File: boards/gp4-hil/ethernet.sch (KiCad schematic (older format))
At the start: 46 parts, among them J1 BEL_FUSE_0826-1G1T-23-F, U2 XC7A100T-1FTG256C, U5 KSZ9031RN, U7 25 MHz

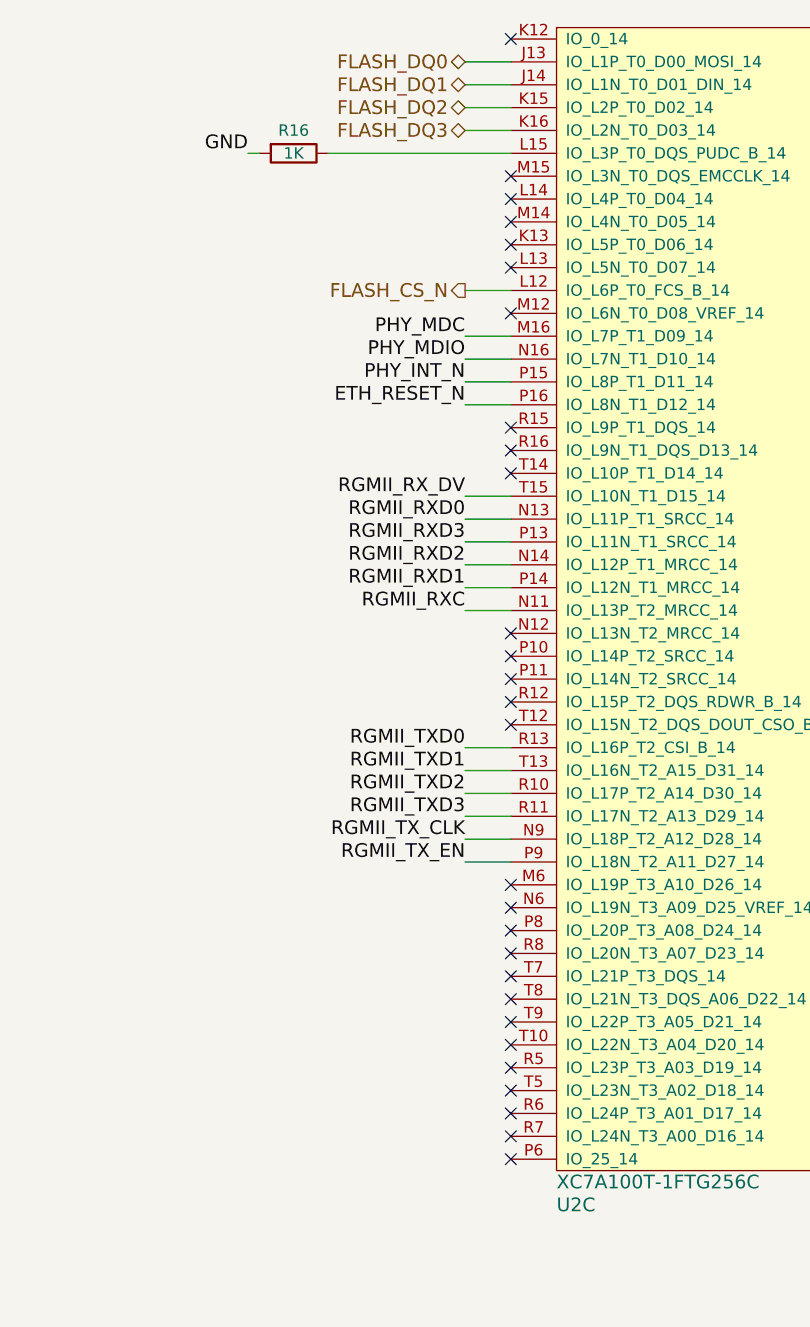
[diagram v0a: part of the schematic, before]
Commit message: Merged JTAG master stuff with Ethernet schematic page
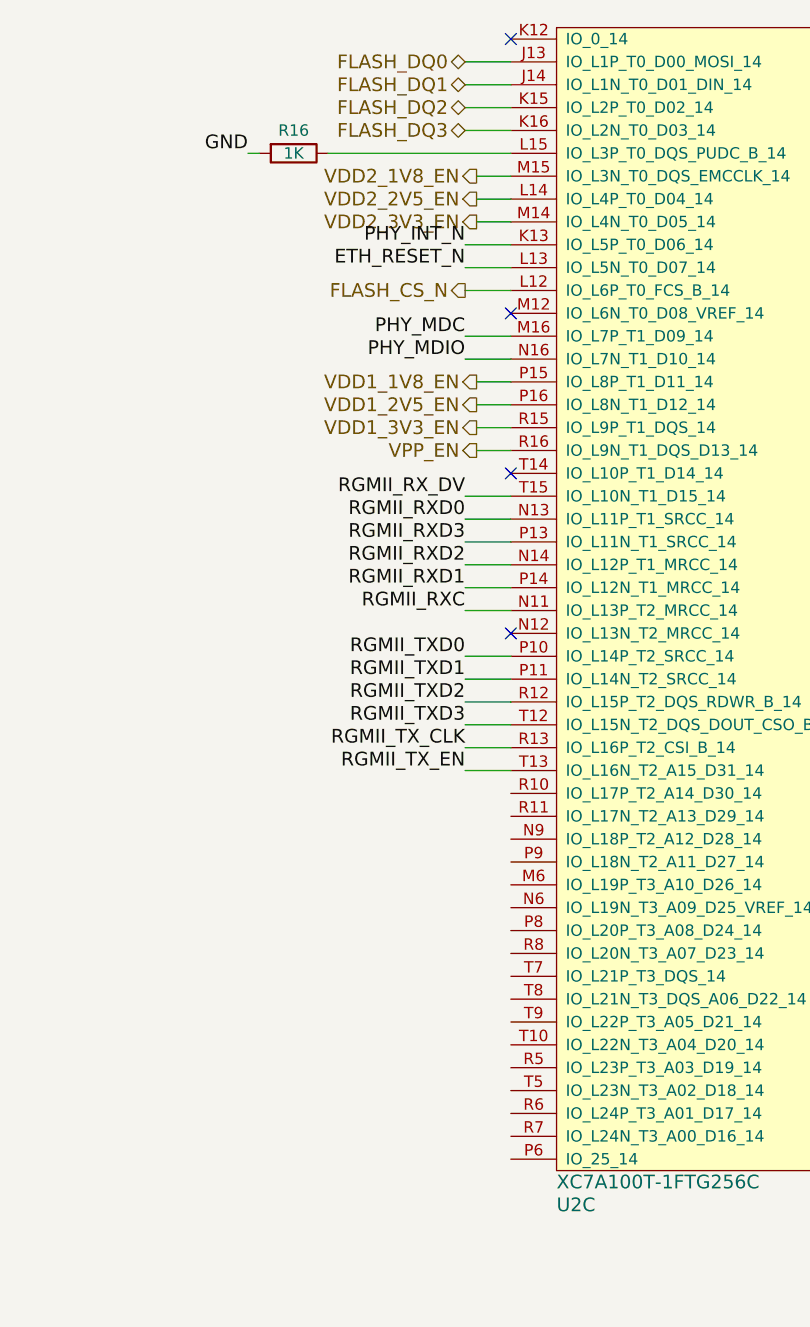
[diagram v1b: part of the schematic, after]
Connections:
- net ETH_RESET_N: now also U2.L13 (IO_L5N_T0_D07_14); no longer U2.P16 (IO_L8N_T1_D12_14)
- net PHY_INT_N: now also U2.K13 (IO_L5P_T0_D06_14); no longer U2.P15 (IO_L8P_T1_D11_14)
- net RGMII_TXD0: now also U2.P10 (IO_L14P_T2_SRCC_14); no longer U2.R13 (IO_L16P_T2_CSI_B_14)
- net RGMII_TXD1: now also U2.P11 (IO_L14N_T2_SRCC_14); no longer U2.T13 (IO_L16N_T2_A15_D31_14)
- net RGMII_TXD2: now also U2.R12 (IO_L15P_T2_DQS_RDWR_B_14); no longer U2.R10 (IO_L17P_T2_A14_D30_14)
- net RGMII_TXD3: now also U2.T12 (IO_L15N_T2_DQS_DOUT_CSO_B_14); no longer U2.R11 (IO_L17N_T2_A13_D29_14)
- net RGMII_TX_CLK: now also U2.R13 (IO_L16P_T2_CSI_B_14); no longer U2.N9 (IO_L18P_T2_A12_D28_14)
- net RGMII_TX_EN: now also U2.T13 (IO_L16N_T2_A15_D31_14); no longer U2.P9 (IO_L18N_T2_A11_D27_14)
- net VDD2_2V5_EN: now reaches U2.L14 (IO_L4P_T0_D04_14)
- net VDD2_3V3_EN: now reaches U2.M14 (IO_L4N_T0_D05_14)
- net VDD2_1V8_EN: now reaches U2.M15 (IO_L3N_T0_DQS_EMCCLK_14)
- net VDD1_3V3_EN: now reaches U2.R15 (IO_L9P_T1_DQS_14)
- net VPP_EN: now reaches U2.R16 (IO_L9N_T1_DQS_D13_14)
- new net VDD1_1V8_EN: U2.P15 (IO_L8P_T1_D11_14)
- new net VDD1_2V5_EN: U2.P16 (IO_L8N_T1_D12_14)
- no-connect marks 31 -> 7
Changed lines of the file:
@@
 $Descr A2 23386 16535
 encoding utf-8
-Sheet 3 8
+Sheet 3 7
 Title "GreenPak Hardware-In-Loop Test Platform"
 Date "2016-05-15"
 Rev "0.1"
 Comp "Andrew Zonenberg"
-Comment1 "Ethernet PHY"
+Comment1 "Ethernet PHY and JTAG masters"
 Comment2 ""
 Comment3 ""
@@
 GND
 Connection ~ 1150 5350
-$Comp
-L XC7AxT-xFTG256x U?
-U 3 1 57349080
-P 16400 9900
-AR Path="/57316B0C/57349080" Ref="U?"  Part="1"
-AR Path="/57316A40/57349080" Ref="U2"  Part="3"
-F 0 "U2" H 16400 9700 60  0000 L CNN
-F 1 "XC7A100T-1FTG256C" H 16400 9800 60  0000 L CNN
-F 2 "" H 16400 9900 60  0000 C CNN
-F 3 "" H 16400 9900 60  0000 C CNN
-	3    16400 9900
-	1    0    0    -1
-$EndComp
 Wire Wire Line
 	8850 8400 8850 8500
@@
 Text Label 16000 6400 2    60   ~ 0
 PHY_MDIO
-Text Label 16000 6500 2    60   ~ 0
+Text Label 16000 5900 2    60   ~ 0
 PHY_INT_N
+Text Label 16000 7700 2    60   ~ 0
+RGMII_TXD0
+Text Label 16000 7800 2    60   ~ 0
+RGMII_TXD1
+Text Label 16000 7900 2    60   ~ 0
+RGMII_TXD2
+Text Label 16000 8000 2    60   ~ 0
+RGMII_TXD3
 Text Label 16000 8100 2    60   ~ 0
-RGMII_TXD0
+RGMII_TX_CLK
 Text Label 16000 8200 2    60   ~ 0
-RGMII_TXD1
-Text Label 16000 8300 2    60   ~ 0
-RGMII_TXD2
-Text Label 16000 8400 2    60   ~ 0
-RGMII_TXD3
-Text Label 16000 8500 2    60   ~ 0
-RGMII_TX_CLK
-Text Label 16000 8600 2    60   ~ 0
 RGMII_TX_EN
-Text Label 16000 6600 2    60   ~ 0
+Text Label 16000 6000 2    60   ~ 0
 ETH_RESET_N
 Wire Wire Line
@@
 Wire Wire Line
 	16000 7000 16200 7000
-NoConn ~ 16200 7600
 Wire Wire Line
 	16000 7400 16200 7400
@@
 	16000 6400 16200 6400
 Wire Wire Line
-	16000 6500 16200 6500
-Wire Wire Line
-	16000 6600 16200 6600
-Wire Wire Line
-	16000 8100 16200 8100
-Wire Wire Line
-	16000 8600 16200 8600
-Wire Wire Line
-	16200 8500 16000 8500
-Wire Wire Line
-	16000 8400 16200 8400
-Wire Wire Line
-	16200 8300 16000 8300
+	16000 5900 16200 5900
+Wire Wire Line
+	16000 6000 16200 6000
+Wire Wire Line
+	16000 7700 16200 7700
 Wire Wire Line
 	16000 8200 16200 8200
-NoConn ~ 16200 5900
-NoConn ~ 16200 5800
-NoConn ~ 16200 5700
-NoConn ~ 16200 5600
-NoConn ~ 16200 6700
-NoConn ~ 16200 6800
+Wire Wire Line
+	16200 8100 16000 8100
+Wire Wire Line
+	16000 8000 16200 8000
+Wire Wire Line
+	16200 7900 16000 7900
+Wire Wire Line
+	16000 7800 16200 7800
 NoConn ~ 16200 6900
-NoConn ~ 16200 9400
-NoConn ~ 16200 9300
-NoConn ~ 16200 9200
-NoConn ~ 16200 9100
-NoConn ~ 16200 9000
-NoConn ~ 16200 8900
-NoConn ~ 16200 8800
-NoConn ~ 16200 8700
 Text Notes 12050 3650 0    60   ~ 0
 TODO: FPGA core clock
@@
 Wire Wire Line
 	16000 6100 16200 6100
-NoConn ~ 16200 6000
 NoConn ~ 16200 6200
-NoConn ~ 16200 8000
-NoConn ~ 16200 7900
-NoConn ~ 16200 7800
-NoConn ~ 16200 7700
-NoConn ~ 16200 9500
-NoConn ~ 16200 9600
-NoConn ~ 16200 9700
-NoConn ~ 16200 9800
-NoConn ~ 16200 9900
+Text HLabel 16050 6700 0    60   Output ~ 0
+VDD1_3V3_EN
+Text HLabel 16050 6600 0    60   Output ~ 0
+VDD1_2V5_EN
+Text HLabel 16050 6500 0    60   Output ~ 0
+VDD1_1V8_EN
+Text HLabel 16050 5800 0    60   Output ~ 0
+VDD2_3V3_EN
+Text HLabel 16050 5700 0    60   Output ~ 0
+VDD2_2V5_EN
+Text HLabel 16050 5600 0    60   Output ~ 0
+VDD2_1V8_EN
+Text HLabel 16050 6800 0    60   Output ~ 0
+VPP_EN
+Wire Wire Line
+	16200 5600 16050 5600
+Wire Wire Line
+	16050 5700 16200 5700
+Wire Wire Line
+	16200 5800 16050 5800
+Wire Wire Line
+	16050 6500 16200 6500
+Wire Wire Line
+	16200 6600 16050 6600
+Wire Wire Line
+	16050 6700 16200 6700
+Wire Wire Line
+	16200 6800 16050 6800
+NoConn ~ 16200 7600
+$Comp
+L XC7AxT-xFTG256x U?
+U 3 1 57349080
+P 16400 9900
+AR Path="/57316B0C/57349080" Ref="U?"  Part="1"
+AR Path="/57316A40/57349080" Ref="U2"  Part="3"
+F 0 "U2" H 16400 9700 60  0000 L CNN
+F 1 "XC7A100T-1FTG256C" H 16400 9800 60  0000 L CNN
+F 2 "" H 16400 9900 60  0000 C CNN
+F 3 "" H 16400 9900 60  0000 C CNN
+	3    16400 9900
+	1    0    0    -1
+$EndComp
 $EndSCHEMATC

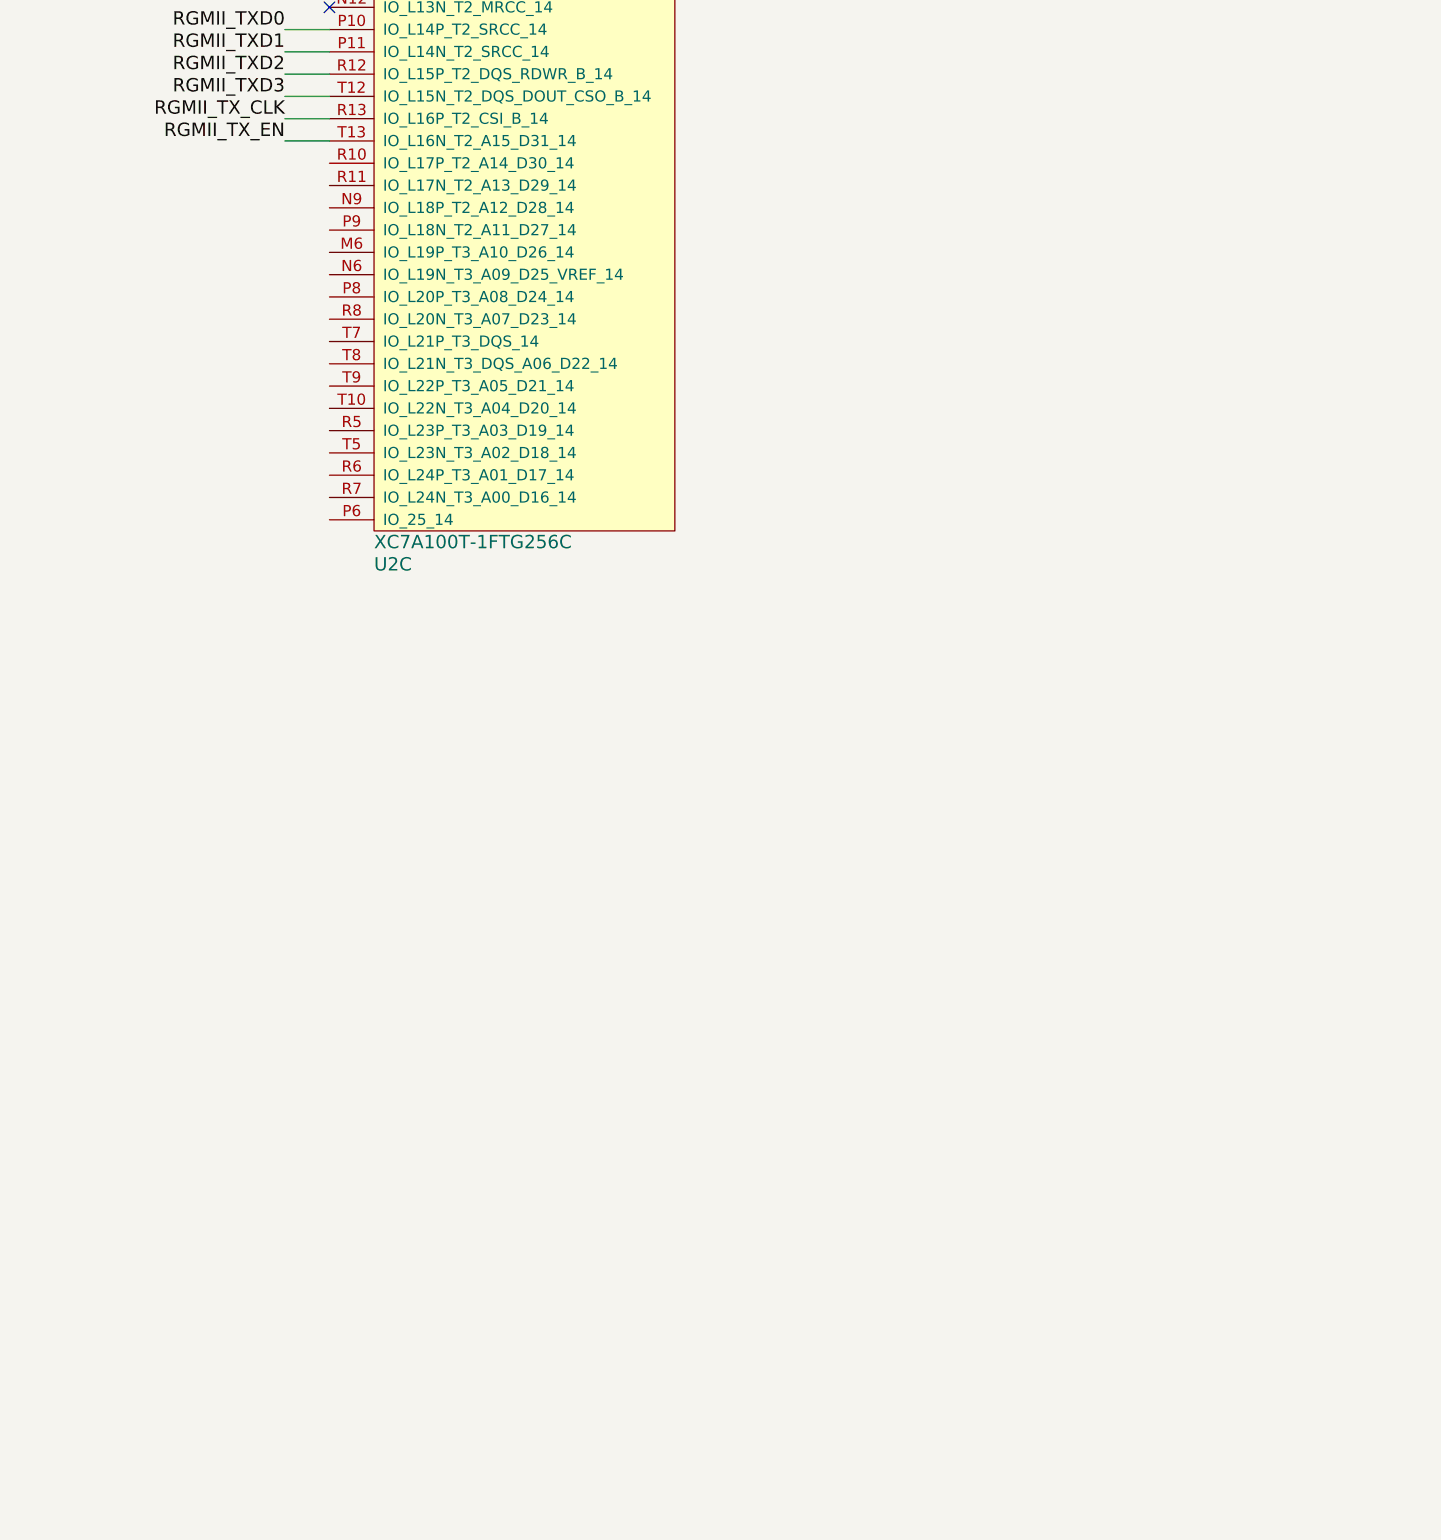
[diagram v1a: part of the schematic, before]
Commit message: Continued schematic capture, added JTAG master interfaces
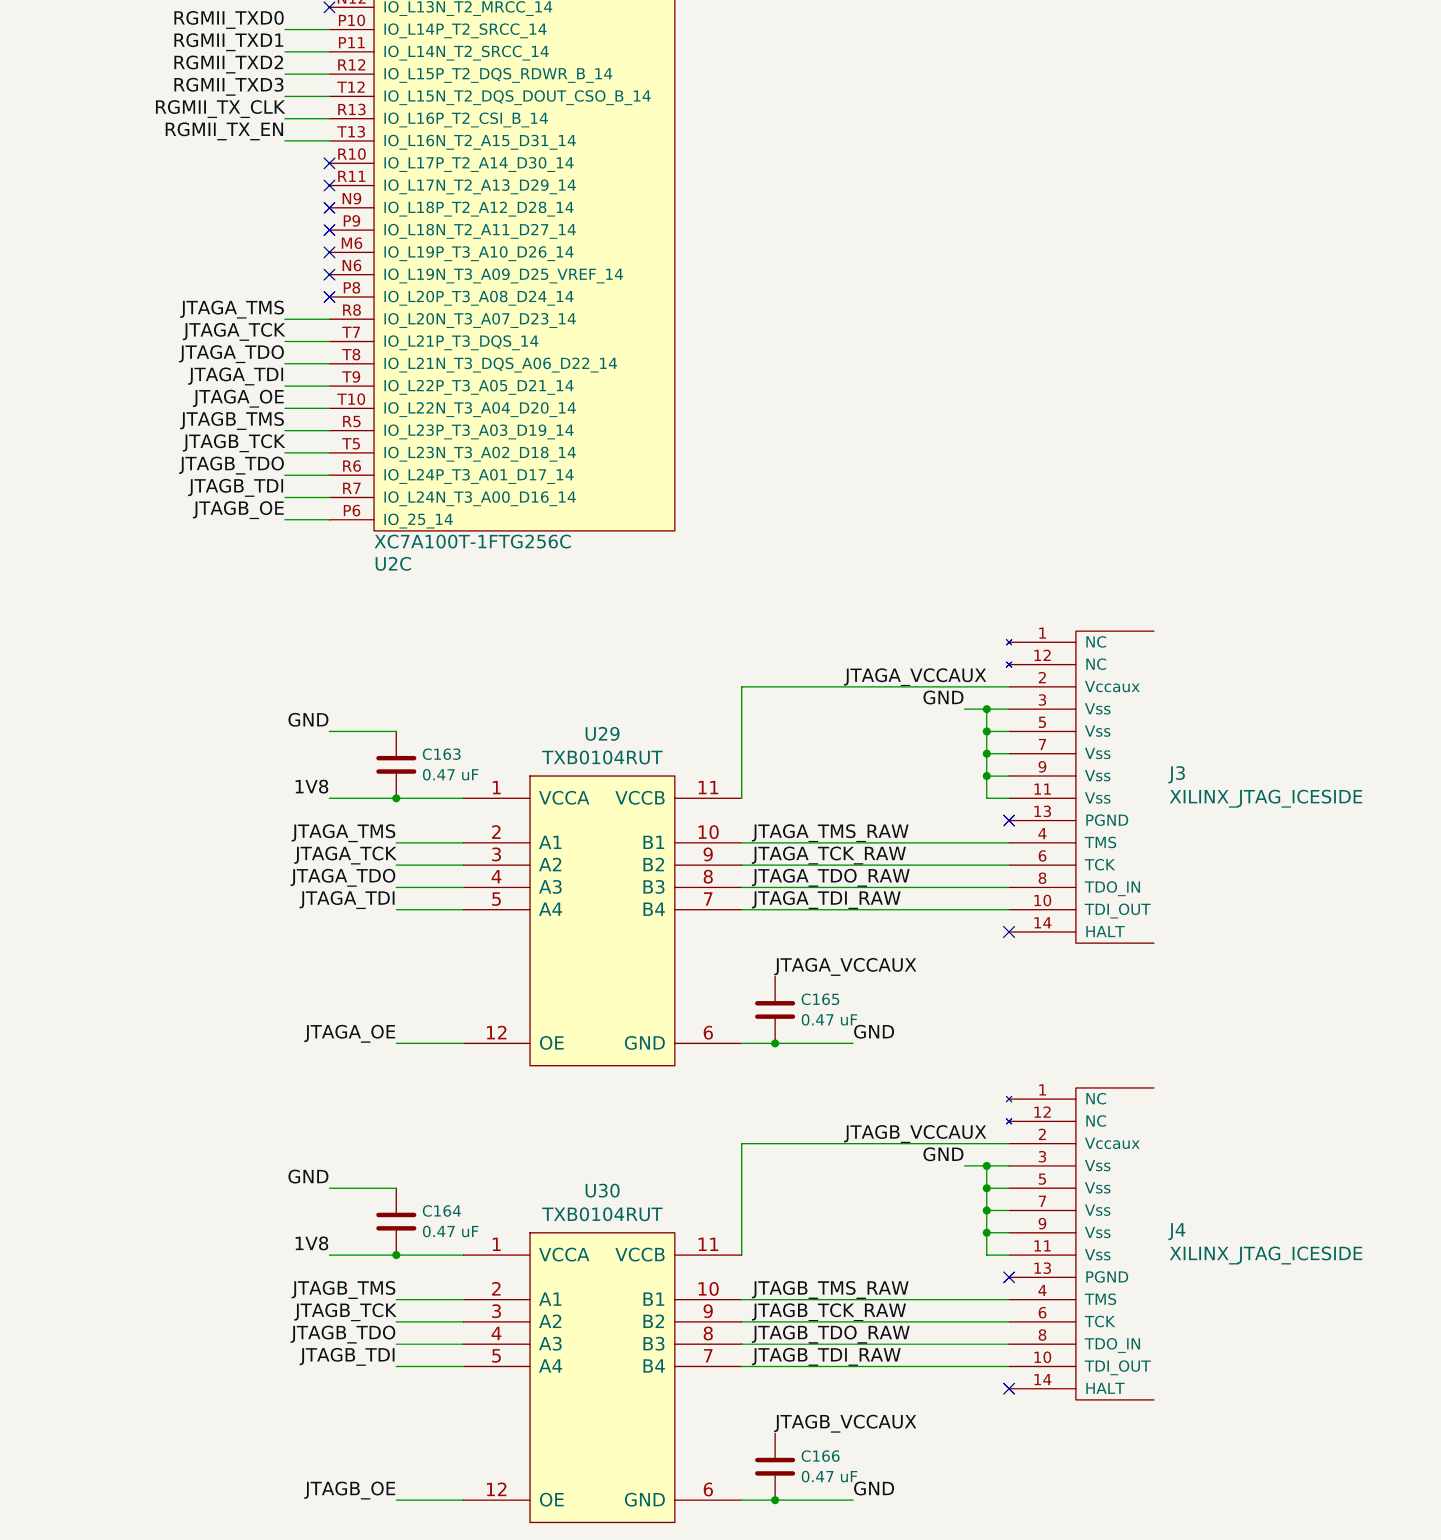
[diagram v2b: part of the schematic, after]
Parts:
- added C163, C164, C165, C166: 0.47 uF, symbol C
- added J3, J4: XILINX_JTAG_ICESIDE, symbol XILINX_JTAG_ICESIDE
- added U29, U30: TXB0104RUT, symbol TXB0104RUT
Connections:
- net 1V8: now also C163.2, C164.2, U29.1 (VCCA), U30.1 (VCCA)
- net GND: now also C163.1, C164.1, C165.2, C166.2, J3.11 (Vss), J3.3 (Vss), J3.5 (Vss), J3.7 (Vss), J3.9 (Vss), J4.11 (Vss), J4.3 (Vss), J4.5 (Vss), J4.7 (Vss), J4.9 (Vss), U29.6 (GND), U30.6 (GND)
- net JTAGB_OE: now reaches U2.P6 (IO_25_14)
- net JTAGB_OE: now also U30.12 (OE)
- net JTAGB_TMS: now reaches U2.R5 (IO_L23P_T3_A03_D19_14)
- net JTAGB_TMS: now also U30.2 (A1)
- net JTAGB_TDO: now reaches U2.R6 (IO_L24P_T3_A01_D17_14)
- net JTAGB_TDO: now also U30.4 (A3)
- net JTAGB_TDI: now reaches U2.R7 (IO_L24N_T3_A00_D16_14)
- net JTAGB_TDI: now also U30.5 (A4)
- net JTAGA_TMS: now reaches U2.R8 (IO_L20N_T3_A07_D23_14)
- net JTAGA_TMS: now also U29.2 (A1)
- net JTAGA_OE: now reaches U2.T10 (IO_L22N_T3_A04_D20_14)
- net JTAGA_OE: now also U29.12 (OE)
- net JTAGB_TCK: now reaches U2.T5 (IO_L23N_T3_A02_D18_14)
- net JTAGB_TCK: now also U30.3 (A2)
- net JTAGA_TCK: now reaches U2.T7 (IO_L21P_T3_DQS_14)
- net JTAGA_TCK: now also U29.3 (A2)
- net JTAGA_TDO: now reaches U2.T8 (IO_L21N_T3_DQS_A06_D22_14)
- net JTAGA_TDO: now also U29.4 (A3)
- net JTAGA_TDI: now reaches U2.T9 (IO_L22P_T3_A05_D21_14)
- net JTAGA_TDI: now also U29.5 (A4)
- new net JTAGA_TCK_RAW: J3.6 (TCK), U29.9 (B2)
- new net JTAGA_TDI_RAW: J3.10 (TDI_OUT), U29.7 (B4)
- new net JTAGA_TDO_RAW: J3.8 (TDO_IN), U29.8 (B3)
- new net JTAGA_TMS_RAW: J3.4 (TMS), U29.10 (B1)
- new net JTAGA_VCCAUX: C165.1, J3.2 (Vccaux), U29.11 (VCCB)
- new net JTAGB_TCK_RAW: J4.6 (TCK), U30.9 (B2)
- new net JTAGB_TDI_RAW: J4.10 (TDI_OUT), U30.7 (B4)
- new net JTAGB_TDO_RAW: J4.8 (TDO_IN), U30.8 (B3)
- new net JTAGB_TMS_RAW: J4.4 (TMS), U30.10 (B1)
- new net JTAGB_VCCAUX: C166.1, J4.2 (Vccaux), U30.11 (VCCB)
- no-connect marks 7 -> 18

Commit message: Added FPGA core clock, GPIO indicator LEDs, expansion header, lots of test points
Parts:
- added C175: 0.47 uF, symbol C
- added R150: 33, symbol R
- added TP22, TP23: TESTPOINT, symbol CONN_01X01
- added U33: 125 MHz, symbol OSC
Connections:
- net 1V8: now also C175.1, U33.1 (E/D#), U33.4 (Vdd)
- net GND: now also C175.2, U33.2 (Vss)
- net PHY_CLK_25MHZ: now also TP22.1 (P1)
- net RGMII_RXD0: now also U2.R16 (IO_L9N_T1_DQS_D13_14); no longer U2.N13 (IO_L11P_T1_SRCC_14)
- net RGMII_RXD1: now also U2.N13 (IO_L11P_T1_SRCC_14); no longer U2.P14 (IO_L12N_T1_MRCC_14)
- net RGMII_RXD2: now also U2.T15 (IO_L10N_T1_D15_14); no longer U2.N14 (IO_L12P_T1_MRCC_14)
- net RGMII_RXD3: now also U2.T14 (IO_L10P_T1_D14_14); no longer U2.P13 (IO_L11N_T1_SRCC_14)
- net RGMII_RX_DV: now also U2.P13 (IO_L11N_T1_SRCC_14); no longer U2.T15 (IO_L10N_T1_D15_14)
- net VDD1_3V3_EN: now also U2.R11 (IO_L17N_T2_A13_D29_14); no longer U2.R15 (IO_L9P_T1_DQS_14)
- net VPP_EN: now also U2.N9 (IO_L18P_T2_A12_D28_14); no longer U2.R16 (IO_L9N_T1_DQS_D13_14)
- net VDD2_EN: now reaches U2.R10 (IO_L17P_T2_A14_D30_14)
- new net: R150.2, U33.3 (CLK)
- new net FPGA_CLK_125MHZ: R150.1, TP23.1 (P1), U2.N14 (IO_L12P_T1_MRCC_14)
- no-connect marks 18 -> 16
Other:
- note removed: "TODO: FPGA core clock"
